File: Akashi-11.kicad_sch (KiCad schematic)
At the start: 42 parts, among them CN10 PPPC192LFBN-RC, CN7 PPPC192LFBN-RC, J1 Conn_02x20_Odd_Even, SW1 SW, U1 MAX6934AQH+D, U2 MAX4719EUB+, U3 TPS613221ADBV, U4 TLV61046ADB

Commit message: Layout refined.
Footprint of L is updated for hand soldering.
Electric Capacitor foot print is now same with EL-210-MOD.
Heater resiters are now same withe EL-210-MOD.
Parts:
- added R6: 18, Capacitor_SMD:C_0603_1608Metric_Pad1.08x0.95mm_HandSolder, symbol Device:R
- C6: value 22u -> UZG0J220MCL1GB; footprint Capacitor_THT:CP_Radial_D5.0mm_P2.50mm -> Capacitor_SMD:CP_Elec_6.3x3
- C9: value 10u -> UZG1H100MCL1GB; footprint Capacitor_THT:CP_Radial_D5.0mm_P2.50mm -> Capacitor_SMD:CP_Elec_4x3.9
- R4: value 39 -> 18
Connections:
- net H2: now also R6.2; no longer U2.9 (COM2)
- new net: R6.1, U2.9 (COM2)
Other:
- moved on the sheet: TP12, TP13
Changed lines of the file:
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@@
   (junction (at 157.48 152.4) (diameter 0) (color 0 0 0 0)
   )
-  (junction (at 85.09 124.46) (diameter 0) (color 0 0 0 0)
-  )
   (junction (at 140.97 152.4) (diameter 0) (color 0 0 0 0)
   )
@@
   (junction (at 36.83 121.92) (diameter 0) (color 0 0 0 0)
   )
+  (junction (at 91.44 124.46) (diameter 0) (color 0 0 0 0)
+  )
   (junction (at 86.36 165.1) (diameter 0) (color 0 0 0 0)
   )
@@
   (junction (at 78.74 135.89) (diameter 0) (color 0 0 0 0)
   )
-  (junction (at 96.52 127) (diameter 0) (color 0 0 0 0)
+  (junction (at 100.33 127) (diameter 0) (color 0 0 0 0)
   )
   (junction (at 207.01 135.89) (diameter 0) (color 0 0 0 0)
@@
     (stroke (width 0) (type default) (color 0 0 0 0))
   )
-  (wire (pts (xy 85.09 124.46) (xy 92.71 124.46))
-    (stroke (width 0) (type default) (color 0 0 0 0))
-  )
   (wire (pts (xy 19.05 129.54) (xy 39.37 129.54))
     (stroke (width 0) (type default) (color 0 0 0 0))
@@
     (stroke (width 0) (type default) (color 0 0 0 0))
   )
-  (wire (pts (xy 76.2 127) (xy 96.52 127))
+  (wire (pts (xy 76.2 127) (xy 100.33 127))
     (stroke (width 0) (type default) (color 0 0 0 0))
   )
@@
     (stroke (width 0) (type default) (color 0 0 0 0))
   )
+  (wire (pts (xy 100.33 125.73) (xy 100.33 127))
+    (stroke (width 0) (type default) (color 0 0 0 0))
+  )
   (wire (pts (xy 177.8 72.39) (xy 186.69 72.39))
     (stroke (width 0) (type default) (color 0 0 0 0))
@@
     (stroke (width 0) (type default) (color 0 0 0 0))
   )
-  (wire (pts (xy 76.2 124.46) (xy 85.09 124.46))
-    (stroke (width 0) (type default) (color 0 0 0 0))
-  )
   (wire (pts (xy 229.87 74.93) (xy 247.65 74.93))
     (stroke (width 0) (type default) (color 0 0 0 0))
@@
     (stroke (width 0) (type default) (color 0 0 0 0))
   )
+  (wire (pts (xy 76.2 124.46) (xy 80.01 124.46))
+    (stroke (width 0) (type default) (color 0 0 0 0))
+  )
   (wire (pts (xy 43.18 161.29) (xy 43.18 165.1))
     (stroke (width 0) (type default) (color 0 0 0 0))
@@
     (stroke (width 0) (type default) (color 0 0 0 0))
   )
-  (wire (pts (xy 96.52 127) (xy 102.87 127))
+  (wire (pts (xy 100.33 127) (xy 102.87 127))
     (stroke (width 0) (type default) (color 0 0 0 0))
   )
@@
     (stroke (width 0) (type default) (color 0 0 0 0))
   )
+  (wire (pts (xy 91.44 124.46) (xy 96.52 124.46))
+    (stroke (width 0) (type default) (color 0 0 0 0))
+  )
   (wire (pts (xy 229.87 67.31) (xy 247.65 67.31))
     (stroke (width 0) (type default) (color 0 0 0 0))
@@
   )
   (wire (pts (xy 260.35 57.15) (xy 274.32 57.15))
+    (stroke (width 0) (type default) (color 0 0 0 0))
+  )
+  (wire (pts (xy 87.63 124.46) (xy 91.44 124.46))
     (stroke (width 0) (type default) (color 0 0 0 0))
   )
@@
     (effects (font (size 1.27 1.27)) (justify left bottom))
   )
-  (label "TIM1_CH1" (at 82.55 127 0)
+  (label "TIM1_CH1" (at 90.17 127 0)
     (effects (font (size 1.27 1.27)) (justify left bottom))
   )
@@
     (effects (font (size 1.27 1.27)) (justify left bottom))
   )
-  (label "H2" (at 88.9 124.46 0)
+  (label "H2" (at 92.71 124.46 0)
     (effects (font (size 1.27 1.27)) (justify left bottom))
   )
@@
       (effects (font (size 1.27 1.27)) (justify left))
     )
-    (property "Value" "22u" (id 1) (at 72.009 172.6061 0)
-      (effects (font (size 1.27 1.27)) (justify left))
-    )
-    (property "Footprint" "Capacitor_THT:CP_Radial_D5.0mm_P2.50mm" (id 2) (at 69.85 171.45 0)
+    (property "Value" "UZG0J220MCL1GB" (id 1) (at 72.009 172.6061 0)
+      (effects (font (size 1.27 1.27)) (justify left))
+    )
+    (property "Footprint" "Capacitor_SMD:CP_Elec_6.3x3" (id 2) (at 69.85 171.45 0)
       (effects (font (size 1.27 1.27)) hide)
     )
@@
     )
     (pin "1")
+  )
+  (symbol (lib_id "Device:R") (at 83.82 124.46 90) (unit 1)
+    (in_bom yes) (on_board yes) (fields_autoplaced)
+    (property "Reference" "R6" (id 0) (at 83.82 119.7442 90))
+    (property "Value" "18" (id 1) (at 83.82 122.2811 90))
+    (property "Footprint" "Capacitor_SMD:C_0603_1608Metric_Pad1.08x0.95mm_HandSolder" (id 2) (at 83.82 126.238 90)
+      (effects (font (size 1.27 1.27)) hide)
+    )
+    (property "Datasheet" "~" (id 3) (at 83.82 124.46 0)
+      (effects (font (size 1.27 1.27)) hide)
+    )
+    (pin "1")
+    (pin "2")
   )
   (symbol (lib_id "Connector:TestPoint") (at 134.62 128.27 0) (unit 1)
@@
     (pin "2")
   )
-  (symbol (lib_id "Connector:TestPoint") (at 96.52 127 0) (unit 1)
+  (symbol (lib_id "Connector:TestPoint") (at 100.33 125.73 0) (unit 1)
     (in_bom yes) (on_board yes)
-    (property "Reference" "TP13" (id 0) (at 97.917 122.8633 0)
-      (effects (font (size 1.27 1.27)) (justify left))
-    )
-    (property "Value" "TestPoint" (id 1) (at 96.52 120.65 0)
-      (effects (font (size 1.27 1.27)) (justify left))
-    )
-    (property "Footprint" "TestPoint:TestPoint_Loop_D1.80mm_Drill1.0mm_Beaded" (id 2) (at 101.6 127 0)
-      (effects (font (size 1.27 1.27)) hide)
-    )
-    (property "Datasheet" "~" (id 3) (at 101.6 127 0)
+    (property "Reference" "TP13" (id 0) (at 101.727 121.5933 0)
+      (effects (font (size 1.27 1.27)) (justify left))
+    )
+    (property "Value" "TestPoint" (id 1) (at 100.33 119.38 0)
+      (effects (font (size 1.27 1.27)) (justify left))
+    )
+    (property "Footprint" "TestPoint:TestPoint_Loop_D1.80mm_Drill1.0mm_Beaded" (id 2) (at 105.41 125.73 0)
+      (effects (font (size 1.27 1.27)) hide)
+    )
+    (property "Datasheet" "~" (id 3) (at 105.41 125.73 0)
       (effects (font (size 1.27 1.27)) hide)
     )
@@
     (in_bom yes) (on_board yes) (fields_autoplaced)
     (property "Reference" "R4" (id 0) (at 33.02 122.2842 90))
-    (property "Value" "39" (id 1) (at 33.02 124.8211 90))
+    (property "Value" "18" (id 1) (at 33.02 124.8211 90))
     (property "Footprint" "Capacitor_SMD:C_0603_1608Metric_Pad1.08x0.95mm_HandSolder" (id 2) (at 33.02 128.778 90)
       (effects (font (size 1.27 1.27)) hide)
@@
       (effects (font (size 1.27 1.27)) (justify left))
     )
-    (property "Value" "10u" (id 1) (at 251.079 145.9361 0)
-      (effects (font (size 1.27 1.27)) (justify left))
-    )
-    (property "Footprint" "Capacitor_THT:CP_Radial_D5.0mm_P2.50mm" (id 2) (at 248.92 144.78 0)
+    (property "Value" "UZG1H100MCL1GB" (id 1) (at 251.079 145.9361 0)
+      (effects (font (size 1.27 1.27)) (justify left))
+    )
+    (property "Footprint" "Capacitor_SMD:CP_Elec_4x3.9" (id 2) (at 248.92 144.78 0)
       (effects (font (size 1.27 1.27)) hide)
     )
@@
     (pin "1")
   )
-  (symbol (lib_id "Connector:TestPoint") (at 85.09 124.46 0) (unit 1)
+  (symbol (lib_id "Connector:TestPoint") (at 91.44 124.46 0) (unit 1)
     (in_bom yes) (on_board yes)
-    (property "Reference" "TP12" (id 0) (at 86.487 120.3233 0)
-      (effects (font (size 1.27 1.27)) (justify left))
-    )
-    (property "Value" "TestPoint" (id 1) (at 82.55 116.84 0)
-      (effects (font (size 1.27 1.27)) (justify left))
-    )
-    (property "Footprint" "TestPoint:TestPoint_Loop_D1.80mm_Drill1.0mm_Beaded" (id 2) (at 90.17 124.46 0)
-      (effects (font (size 1.27 1.27)) hide)
-    )
-    (property "Datasheet" "~" (id 3) (at 90.17 124.46 0)
+    (property "Reference" "TP12" (id 0) (at 92.837 120.3233 0)
+      (effects (font (size 1.27 1.27)) (justify left))
+    )
+    (property "Value" "TestPoint" (id 1) (at 88.9 116.84 0)
+      (effects (font (size 1.27 1.27)) (justify left))
+    )
+    (property "Footprint" "TestPoint:TestPoint_Loop_D1.80mm_Drill1.0mm_Beaded" (id 2) (at 96.52 124.46 0)
+      (effects (font (size 1.27 1.27)) hide)
+    )
+    (property "Datasheet" "~" (id 3) (at 96.52 124.46 0)
       (effects (font (size 1.27 1.27)) hide)
     )
@@
     )
     (path "/746d5d6e-d183-4a43-98fc-0910c3a56939"
-      (reference "C6") (unit 1) (value "22u") (footprint "Capacitor_THT:CP_Radial_D5.0mm_P2.50mm")
+      (reference "C6") (unit 1) (value "UZG0J220MCL1GB") (footprint "Capacitor_SMD:CP_Elec_6.3x3")
     )
     (path "/03f09313-6917-4cb7-9358-3b4f9e115ab2"
@@
     )
     (path "/ce4a2bdc-5956-467a-becf-ee6582a3ff8f"
-      (reference "C9") (unit 1) (value "10u") (footprint "Capacitor_THT:CP_Radial_D5.0mm_P2.50mm")
+      (reference "C9") (unit 1) (value "UZG1H100MCL1GB") (footprint "Capacitor_SMD:CP_Elec_4x3.9")
     )
     (path "/00000000-0000-0000-0000-00005c96bbda"
@@
     )
     (path "/aa7e72ca-4dfc-42eb-9354-239397f2ab9c"
-      (reference "R4") (unit 1) (value "39") (footprint "Capacitor_SMD:C_0603_1608Metric_Pad1.08x0.95mm_HandSolder")
+      (reference "R4") (unit 1) (value "18") (footprint "Capacitor_SMD:C_0603_1608Metric_Pad1.08x0.95mm_HandSolder")
     )
     (path "/df2d9c9f-cb48-424c-9647-501642b6bc8d"
       (reference "R5") (unit 1) (value "330") (footprint "Capacitor_SMD:C_0603_1608Metric_Pad1.08x0.95mm_HandSolder")
     )
+    (path "/8ce81ab9-7f4c-4250-a09f-443d5117f2dc"
+      (reference "R6") (unit 1) (value "18") (footprint "Capacitor_SMD:C_0603_1608Metric_Pad1.08x0.95mm_HandSolder")
+    )
     (path "/a1fa917d-ac5c-4551-81b6-88418e5c28d1"

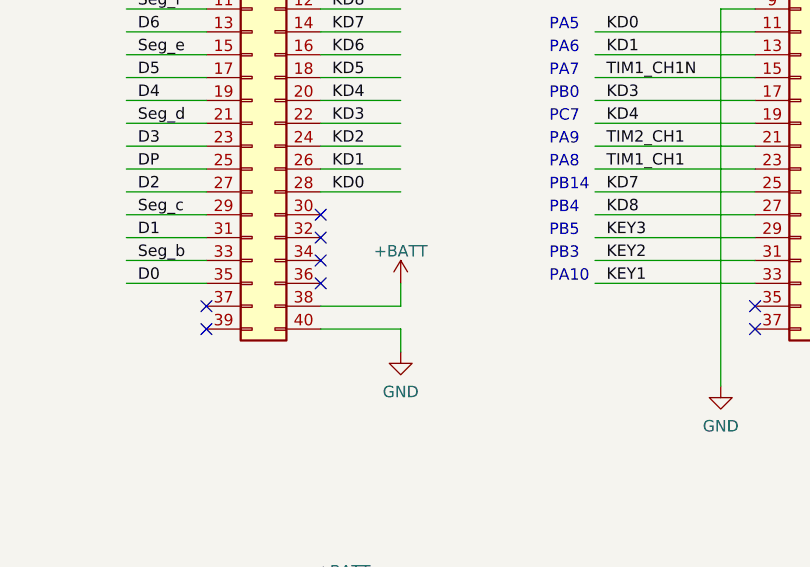
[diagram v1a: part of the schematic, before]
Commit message: Add current measurment point
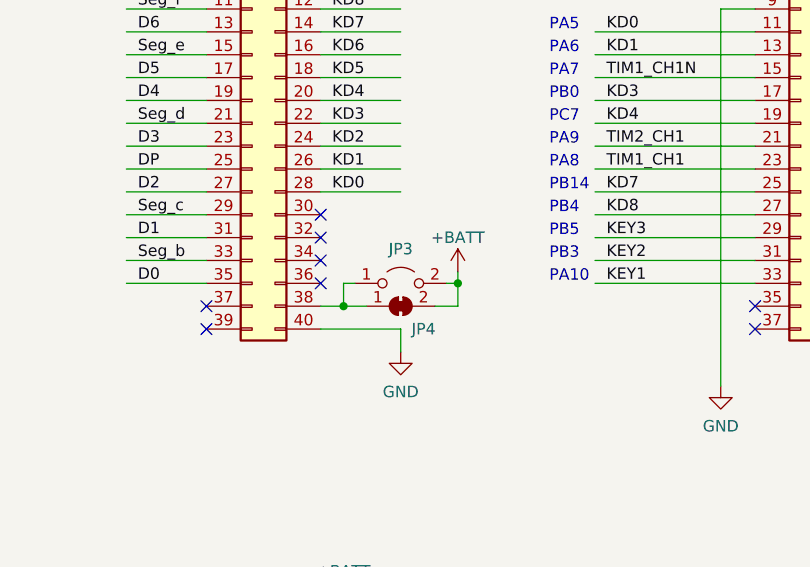
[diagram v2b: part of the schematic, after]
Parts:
- added JP3: Jumper_2_Open, Connector_PinHeader_2.54mm:PinHeader_1x02_P2.54mm_Vertical, symbol Jumper:Jumper_2_Open
- added JP4: SolderJumper_2_Bridged, Jumper:SolderJumper-2_P1.3mm_Bridged_RoundedPad1.0x1.5mm, symbol Jumper:SolderJumper_2_Bridged
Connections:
- net +BATT: now also JP3.2 (B), JP4.2 (B); no longer J1.38 (Pin_38)
- new net: J1.38 (Pin_38), JP3.1 (A), JP4.1 (A)
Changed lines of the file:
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@@
   (junction (at 248.92 132.08) (diameter 0) (color 0 0 0 0)
   )
+  (junction (at 214.63 80.01) (diameter 0) (color 0 0 0 0)
+  )
   (junction (at 55.88 66.04) (diameter 0) (color 0 0 0 0)
   )
@@
   )
   (junction (at 100.33 127) (diameter 0) (color 0 0 0 0)
+  )
+  (junction (at 201.93 82.55) (diameter 0) (color 0 0 0 0)
   )
   (junction (at 207.01 135.89) (diameter 0) (color 0 0 0 0)
@@
   (no_connect (at 92.71 74.93))
   (no_connect (at 92.71 69.85))
+  (wire (pts (xy 214.63 80.01) (xy 214.63 82.55))
+    (stroke (width 0) (type default) (color 0 0 0 0))
+  )
   (wire (pts (xy 167.64 149.86) (xy 167.64 152.4))
     (stroke (width 0) (type default) (color 0 0 0 0))
@@
     (stroke (width 0) (type default) (color 0 0 0 0))
   )
+  (wire (pts (xy 212.09 82.55) (xy 214.63 82.55))
+    (stroke (width 0) (type default) (color 0 0 0 0))
+  )
   (wire (pts (xy 91.44 161.29) (xy 91.44 165.1))
     (stroke (width 0) (type default) (color 0 0 0 0))
@@
     (stroke (width 0) (type default) (color 0 0 0 0))
   )
-  (wire (pts (xy 199.39 82.55) (xy 208.28 82.55))
+  (wire (pts (xy 199.39 82.55) (xy 201.93 82.55))
     (stroke (width 0) (type default) (color 0 0 0 0))
   )
@@
     (stroke (width 0) (type default) (color 0 0 0 0))
   )
+  (wire (pts (xy 201.93 80.01) (xy 201.93 82.55))
+    (stroke (width 0) (type default) (color 0 0 0 0))
+  )
   (wire (pts (xy 199.39 41.91) (xy 208.28 41.91))
     (stroke (width 0) (type default) (color 0 0 0 0))
@@
     (stroke (width 0) (type default) (color 0 0 0 0))
   )
+  (wire (pts (xy 201.93 82.55) (xy 204.47 82.55))
+    (stroke (width 0) (type default) (color 0 0 0 0))
+  )
   (wire (pts (xy 260.35 67.31) (xy 274.32 67.31))
     (stroke (width 0) (type default) (color 0 0 0 0))
@@
     (stroke (width 0) (type default) (color 0 0 0 0))
   )
-  (wire (pts (xy 208.28 80.01) (xy 208.28 82.55))
+  (wire (pts (xy 214.63 78.74) (xy 214.63 80.01))
     (stroke (width 0) (type default) (color 0 0 0 0))
   )
@@
     (stroke (width 0) (type default) (color 0 0 0 0))
   )
+  (wire (pts (xy 203.2 80.01) (xy 201.93 80.01))
+    (stroke (width 0) (type default) (color 0 0 0 0))
+  )
   (wire (pts (xy 138.43 41.91) (xy 151.13 41.91))
     (stroke (width 0) (type default) (color 0 0 0 0))
@@
   )
   (wire (pts (xy 201.93 134.62) (xy 201.93 135.89))
+    (stroke (width 0) (type default) (color 0 0 0 0))
+  )
+  (wire (pts (xy 213.36 80.01) (xy 214.63 80.01))
     (stroke (width 0) (type default) (color 0 0 0 0))
   )
@@
     )
     (pin "1")
+  )
+  (symbol (lib_id "Jumper:Jumper_2_Open") (at 208.28 80.01 0) (unit 1)
+    (in_bom yes) (on_board yes) (fields_autoplaced)
+    (property "Reference" "JP3" (id 0) (at 208.28 76.2 0))
+    (property "Value" "Jumper_2_Open" (id 1) (at 208.28 76.2 0)
+      (effects (font (size 1.27 1.27)) hide)
+    )
+    (property "Footprint" "Connector_PinHeader_2.54mm:PinHeader_1x02_P2.54mm_Vertical" (id 2) (at 208.28 80.01 0)
+      (effects (font (size 1.27 1.27)) hide)
+    )
+    (property "Datasheet" "~" (id 3) (at 208.28 80.01 0)
+      (effects (font (size 1.27 1.27)) hide)
+    )
+    (pin "1")
+    (pin "2")
   )
   (symbol (lib_id "Connector:TestPoint") (at 27.94 127 0) (unit 1)
@@
     )
     (property "Datasheet" "~" (id 3) (at 152.4 26.67 0)
+      (effects (font (size 1.27 1.27)) hide)
+    )
+    (pin "1")
+    (pin "2")
+  )
+  (symbol (lib_id "Jumper:SolderJumper_2_Bridged") (at 208.28 82.55 0) (unit 1)
+    (in_bom yes) (on_board yes)
+    (property "Reference" "JP4" (id 0) (at 210.82 85.09 0))
+    (property "Value" "SolderJumper_2_Bridged" (id 1) (at 208.28 78.74 0)
+      (effects (font (size 1.27 1.27)) hide)
+    )
+    (property "Footprint" "Jumper:SolderJumper-2_P1.3mm_Bridged_RoundedPad1.0x1.5mm" (id 2) (at 208.28 82.55 0)
+      (effects (font (size 1.27 1.27)) hide)
+    )
+    (property "Datasheet" "~" (id 3) (at 208.28 82.55 0)
       (effects (font (size 1.27 1.27)) hide)
     )
@@
     (pin "1")
   )
-  (symbol (lib_id "power:+BATT") (at 208.28 80.01 0) (unit 1)
-    (in_bom yes) (on_board yes) (fields_autoplaced)
-    (property "Reference" "#PWR029" (id 0) (at 208.28 83.82 0)
-      (effects (font (size 1.27 1.27)) hide)
-    )
-    (property "Value" "+BATT" (id 1) (at 208.28 76.4342 0))
-    (property "Footprint" "" (id 2) (at 208.28 80.01 0)
-      (effects (font (size 1.27 1.27)) hide)
-    )
-    (property "Datasheet" "" (id 3) (at 208.28 80.01 0)
+  (symbol (lib_id "power:+BATT") (at 214.63 78.74 0) (unit 1)
+    (in_bom yes) (on_board yes)
+    (property "Reference" "#PWR029" (id 0) (at 214.63 82.55 0)
+      (effects (font (size 1.27 1.27)) hide)
+    )
+    (property "Value" "+BATT" (id 1) (at 214.63 74.93 0))
+    (property "Footprint" "" (id 2) (at 214.63 78.74 0)
+      (effects (font (size 1.27 1.27)) hide)
+    )
+    (property "Datasheet" "" (id 3) (at 214.63 78.74 0)
       (effects (font (size 1.27 1.27)) hide)
     )
@@
       (reference "JP2") (unit 1) (value "Jumper_2_Bridged") (footprint "Jumper:SolderJumper-2_P1.3mm_Bridged_RoundedPad1.0x1.5mm")
     )
+    (path "/4d73afef-3e12-4b64-be10-a6c5f9031031"
+      (reference "JP3") (unit 1) (value "Jumper_2_Open") (footprint "Connector_PinHeader_2.54mm:PinHeader_1x02_P2.54mm_Vertical")
+    )
+    (path "/a5383d44-32d8-44f2-a3a5-b237ee8f7f39"
+      (reference "JP4") (unit 1) (value "SolderJumper_2_Bridged") (footprint "Jumper:SolderJumper-2_P1.3mm_Bridged_RoundedPad1.0x1.5mm")
+    )
     (path "/f2deddfd-89b8-4596-90ac-4edc0864ba22"

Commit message: Changed from Nucleo to RPi Pico
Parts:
- removed CN10, CN7: PPPC192LFBN-RC, Connector_PinSocket_2.54mm:PinSocket_2x19_P2.54mm_Vertical, symbol Connector_Generic:Conn_02x19_Odd_Even
- removed D3: LED, LED_THT:LED_D4.0mm, symbol Device:LED
- removed R1: 1k, Capacitor_SMD:C_0603_1608Metric_Pad1.08x0.95mm_HandSolder, symbol Device:R
- removed SW1: SW, Button_Switch_THT:SW_TH_Tactile_Omron_B3F-10xx, symbol Switch:SW_MEC_5G
- added D3: D_Schottky, Diode_SMD:D_0603_1608Metric_Pad1.05x0.95mm_HandSolder, symbol Device:D_Schottky
- added SW1: SW_MEC_5E, Button_Switch_THT:SW_TH_Tactile_Omron_B3F-10xx, symbol Switch:SW_MEC_5E
- added U5: Pico, RPi_Pico:RPi_Pico_SMD_TH, symbol RPI_PICO:Pico
- D1, D2: footprint Capacitor_SMD:C_0603_1608Metric_Pad1.08x0.95mm_HandSolder -> Diode_SMD:D_0603_1608Metric_Pad1.05x0.95mm_HandSolder
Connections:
- net +BATT: now also D3.2 (A)
- net BLANK: now also U5.21 (GPIO16)
- net D0: now also U1.25 (OUT15); no longer U1.42 (OUT0)
- net D1: now also U1.27 (OUT13); no longer U1.40 (OUT2)
- net D2: now also U1.30 (OUT12); no longer U1.38 (OUT4)
- net D3: now also U1.33 (OUT9); no longer U1.36 (OUT6)
- net D4: now also U1.35 (OUT7); no longer U1.34 (OUT8)
- net D5: now also U1.36 (OUT6); no longer U1.33 (OUT9)
- net D7: now also U1.40 (OUT2); no longer U1.27 (OUT13)
- net D8: now also U1.42 (OUT0); no longer U1.25 (OUT15)
- net DP: now also U1.32 (OUT10); no longer U1.37 (OUT5)
- net GND: now also SW1.3 (K), SW1.4 (A), U5.13 (GND), U5.18 (GND), U5.23 (GND), U5.28 (GND), U5.3 (GND), U5.33 (AGND), U5.38 (GND), U5.8 (GND)
- net KD0: now also U5.15 (GPIO11)
- net KD1: now also U5.14 (GPIO10)
- net KD2: now also U5.12 (GPIO9)
- net KD3: now also U5.11 (GPIO8)
- net KD4: now also U5.10 (GPIO7)
- net KD5: now also U5.9 (GPIO6)
- net KD6: now also U5.7 (GPIO5)
- net KD7: now also U5.6 (GPIO4)
- net KD8: now also U5.5 (GPIO3)
- net KEY1: now also U5.1 (GPIO0)
- net KEY2: now also U5.2 (GPIO1)
- net KEY3: now also U5.4 (GPIO2)
- net LOAD: now also U5.22 (GPIO17)
- net Seg_a: now also U1.3 (OUT31); no longer U1.20 (OUT16)
- net Seg_b: now also U1.26 (OUT14); no longer U1.41 (OUT1)
- net Seg_c: now also U1.38 (OUT4); no longer U1.39 (OUT3)
- net Seg_d: now also U1.34 (OUT8); no longer U1.35 (OUT7)
- net Seg_e: now also U1.37 (OUT5); no longer U1.32 (OUT10)
- net Seg_f: now also U1.39 (OUT3); no longer U1.30 (OUT12)
- net Seg_g: now also U1.41 (OUT1); no longer U1.26 (OUT14)
- net SPI1_MOSI renamed MOSI
- net MOSI: now also U5.25 (GPIO19)
- net SPI1_SCK renamed SCK
- net SCK: now also U5.24 (GPIO18)
- net TIM1_CH1 renamed H_PWM_P
- net H_PWM_P: now also U5.16 (GPIO12)
- net TIM1_CH1N renamed H_PWM_N
- net H_PWM_N: now also U5.17 (GPIO13)
- net TIM2_CH1 renamed CHARGE_P_PWM
- net CHARGE_P_PWM: now also U5.26 (GPIO20)
- new net: SW1.1, SW1.2, U5.30 (RUN)
- new net: D3.1 (K), U5.39 (VSYS)
- new net EN24V: U5.27 (GPIO21)
- no-connect marks 68 -> 36
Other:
- note removed: "PA10"
- note removed: "PA12"
- note removed: "PA5"
- note removed: "PA6"
- note removed: "PA7"
- note removed: "PA8"
- note removed: "PA9"
- note removed: "PB0"
- note removed: "PB14"
- note removed: "PB2"
- note removed: "PB3"
- note removed: "PB4"
- note removed: "PB5"
- note removed: "PB6"
- note removed: "PC1"
- note removed: "PC10"
- note removed: "PC12"
- note removed: "PC7"
- note removed: "PD8"
- note removed: "STATUS"
- moved on the sheet: C3, C5, C8, J1, JP3, JP4, TP2, U1
